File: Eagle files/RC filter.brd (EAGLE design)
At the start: 7.6 x 22.9 mm, 4 parts

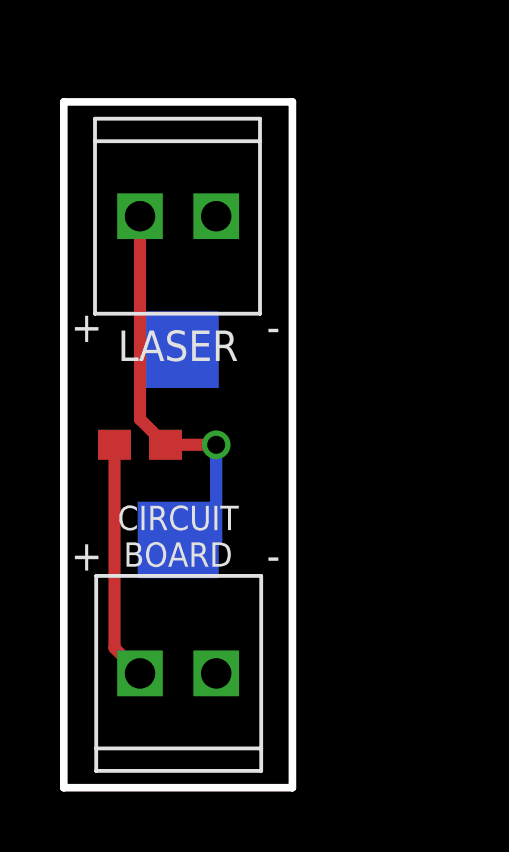
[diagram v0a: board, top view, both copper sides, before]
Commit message: Changed screw terminal to 5.08 mm layout
Bumped board to v1.1
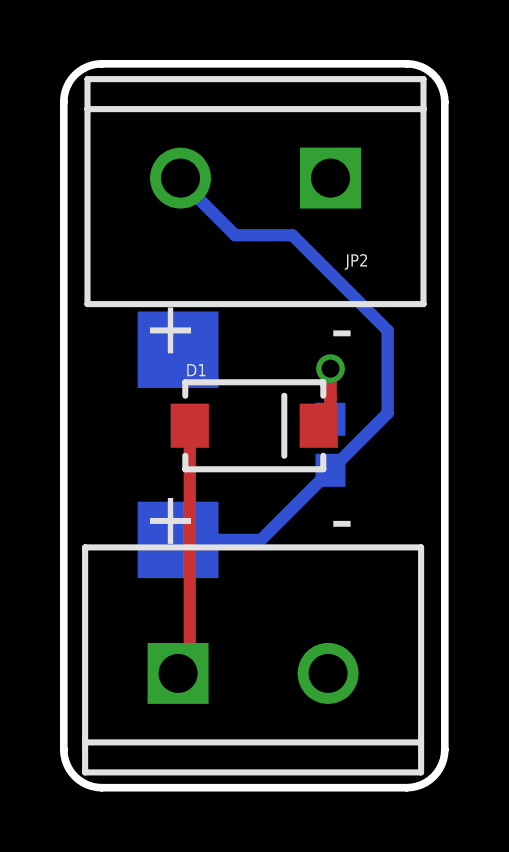
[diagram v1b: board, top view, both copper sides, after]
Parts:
- added D1: (no value), SparkFun-DiscreteSemi:SMA-DIODE
- JP2, TO_CB: value M022.54MM_SCREWTERM -> M025MM; device SparkFun-Connectors:1X02_2.54_SCREWTERM -> SparkFun-Connectors:SCREWTERMINAL-5MM-2
- moved JP2 6.48 mm to (8.89, 20.3), turned to 180 degrees
- moved R1 6.35 mm to (8.89, 11.4), flipped to the bottom, turned to 90 degrees
- moved TO_CB 1.27 mm to (3.81, 3.81), turned to 0 degrees
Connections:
- removed net N$2: C1.A, JP2.P2, R1.1
- new net V_IN: D1.A, TO_CB.1
- new net V_OUT: C1.A, JP2.2, R1.1
- net GND: now also JP2.1, TO_CB.2; no longer JP2.P1, TO_CB.P2
- net N$1: now also D1.C; no longer TO_CB.P1
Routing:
- net V_OUT: track 0.00 -> 20.5 mm
- net N$2: track 15.0 -> 0.00 mm, vias 1 -> 0
- net V_IN: track 0.00 -> 8.42 mm
- net N$1: track 7.97 -> 3.68 mm, vias 0 -> 1
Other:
- board size 7.6 x 22.9 mm -> 12.7 x 24.1 mm
- board text added: "v1.1"
- board text removed: "GND"
- board text removed: "v1.0"
